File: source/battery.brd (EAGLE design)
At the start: 29.9 x 20.6 mm, 21 parts, among them SW1 SWITCH, U1 TP5410

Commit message: Update source to v11 of the project
Minor updates.
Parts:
- BAT+, U$5: device battery:PIN -> alim:PIN
- C1, C2, C3, C4: device battery:CAPC2214X120 -> alim:CAPC2214X120
- C5, C6: device battery:CAPC1508X45 -> alim:CAPC1508X45
- D1: device battery:DIOM6859X265 -> alim:DIOM6859X265
- I1: device battery:DR73 -> alim:DR73
- LD1: device battery:LEDBI0603 -> alim:LEDBI0603
- LD2: device battery:SML1206 -> alim:SML1206
- R1, R3, R5: device battery:RESC1508X30 -> alim:RESC1508X30
- R2: device battery:RESC3116X40 -> alim:RESC3116X40
- SW1: device battery:BUTTON -> alim:BUTTON
- U$1: device battery:USB20 -> alim:USB20
- U$3: device battery:MICRO-USB -> alim:MICRO-USB
- U1: device battery:SOIC127P600X175-8 -> alim:SOIC127P600X175-8
- moved SW1 2.80 mm to (3.20, 19.9)
- moved R2 0.25 mm to (2.85, 14.6)
- moved U$5 0.15 mm to (7.89, 10.1)
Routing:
- net N$5: track 0.00 -> 12.1 mm
- net N$14: track 0.00 -> 5.20 mm
- net N$16: track 0.00 -> 5.10 mm
- net N$7: track 0.00 -> 4.90 mm
- net N$13: track 0.00 -> 4.85 mm
- net N$4: track 0.00 -> 4.50 mm
- net N$6: track 0.00 -> 4.30 mm
- net N$17: track 0.00 -> 4.30 mm
- net +5V: track 37.8 -> 41.5 mm
- net N$8: track 0.00 -> 3.55 mm
- net N$10: track 0.00 -> 2.70 mm
- net N$9: track 0.00 -> 2.50 mm
- net N$15: track 0.00 -> 2.40 mm
- net N$2: track 3.24 -> 5.08 mm
- net N$3: track 2.89 -> 4.27 mm
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
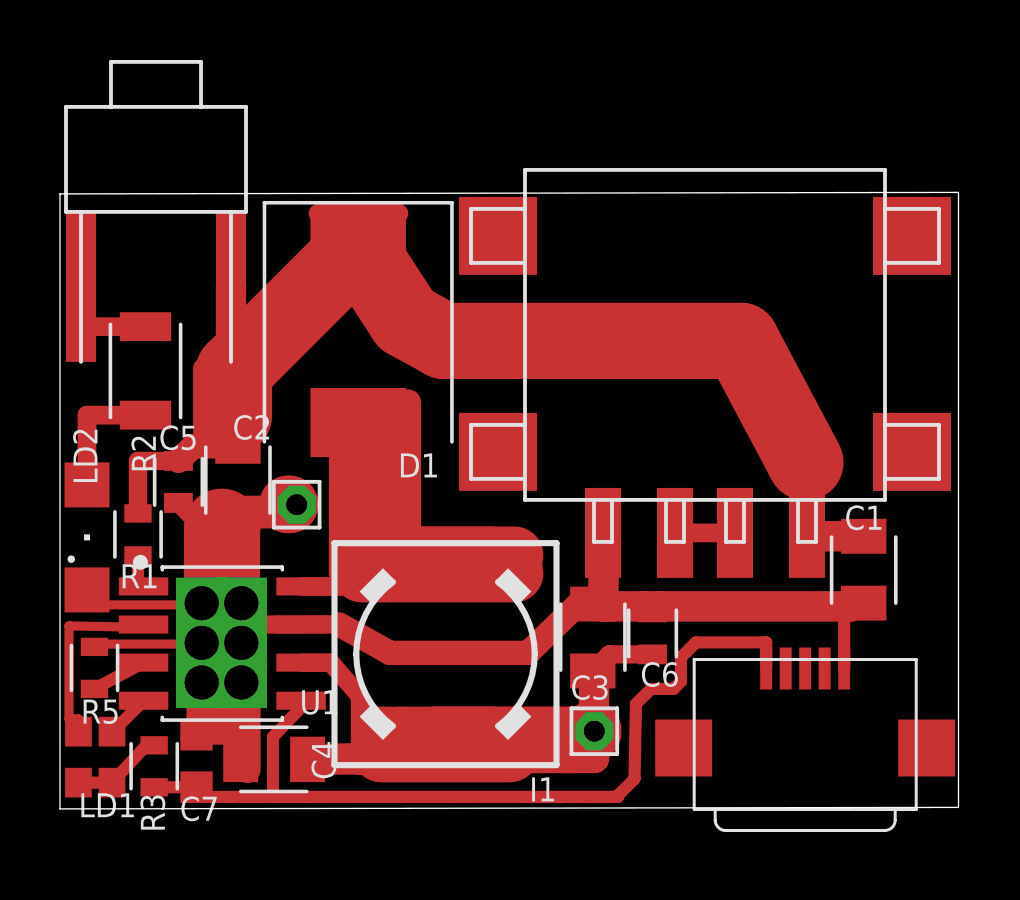
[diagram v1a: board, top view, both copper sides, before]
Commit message: Update to v12 of the project
This slightly rearranges certain tracks to ease laser engraving,
manual components placement and soldering.
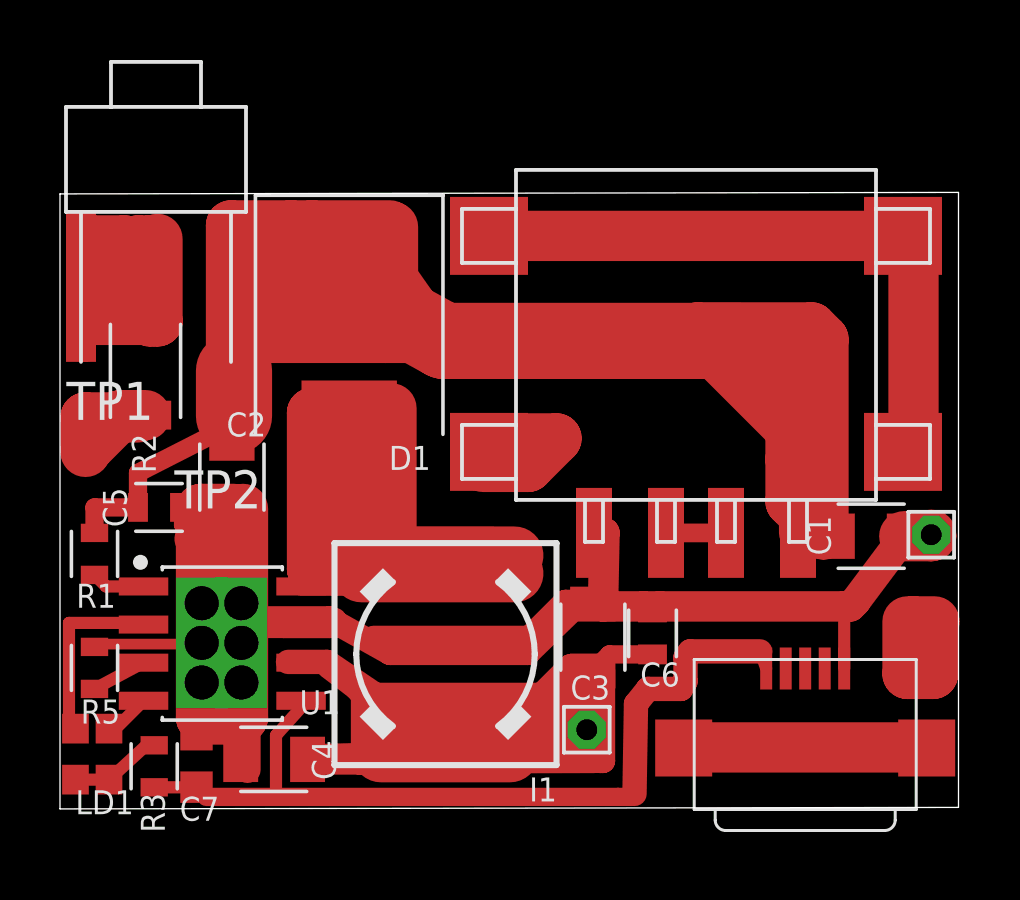
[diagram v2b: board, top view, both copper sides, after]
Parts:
- removed LD2: LED_POWER, alim:SML1206
- added TP1, TP2: TPB1,27, testpad:B1,27
- moved U$5 21.2 mm to (29.0, 9.14)
- moved R1 1.59 mm to (1.15, 8.50)
- moved C1 1.16 mm to (27.0, 9.09), turned to 0 degrees
- moved C5 1.07 mm to (3.30, 10.1), turned to 0 degrees
- moved D1 0.39 mm to (9.64, 16.1)
- moved U$1 0.30 mm to (21.2, 15.8)
- moved BAT+ 0.25 mm to (17.6, 2.64)
- moved C2 0.22 mm to (5.73, 11.1)
- moved LD1 0.14 mm to (1.10, 1.80)
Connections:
- net GND: now also TP2.TP; no longer LD2.C
- net N$3: now also TP1.TP; no longer LD2.A
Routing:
- net N$35: track 0.00 -> 23.9 mm
- net N$20: track 0.00 -> 21.1 mm
- net N$28: track 0.00 -> 16.6 mm
- net N$11: track 0.05 -> 14.2 mm
- net N$9: track 2.50 -> 16.4 mm
- net N$37: track 0.00 -> 12.5 mm
- net N$5: track 12.1 -> 0.00 mm
- net N$23: track 0.00 -> 11.7 mm
- net N$7: track 4.90 -> 14.6 mm
- net N$21: track 0.00 -> 8.30 mm
- net N$29: track 0.00 -> 8.00 mm
- net GND: track 57.4 -> 50.9 mm
- net N$27: track 0.00 -> 6.15 mm
- net LX: track 10.8 -> 5.12 mm
- net N$31: track 0.00 -> 5.45 mm
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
